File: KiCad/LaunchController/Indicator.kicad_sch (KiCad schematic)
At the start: 73 parts

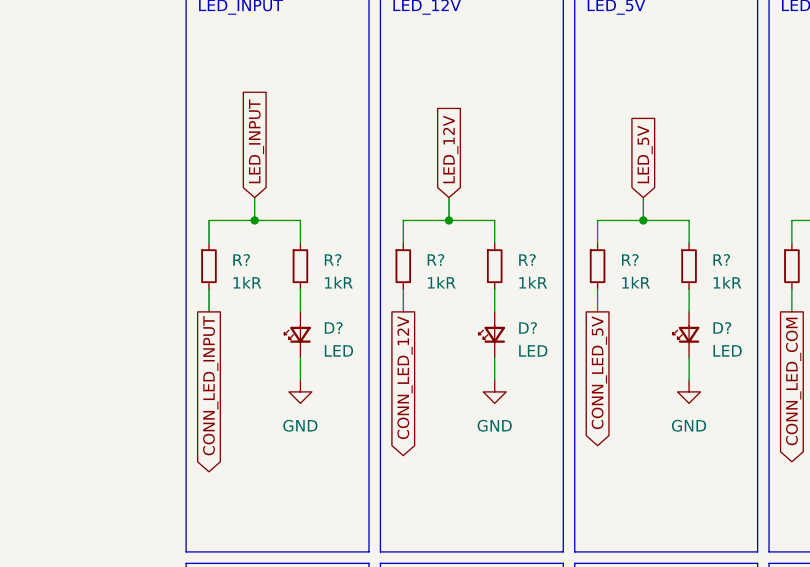
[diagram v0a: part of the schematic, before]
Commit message: 電圧から抵抗値を修正
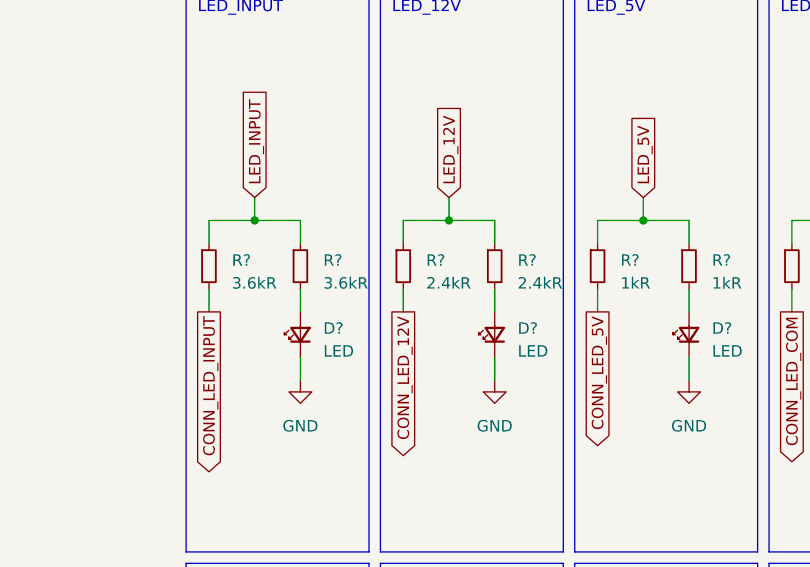
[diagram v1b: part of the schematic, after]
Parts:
- R? (x2): value 1kR -> 3.6kR
- R? (x2): value 1kR -> 2.4kR
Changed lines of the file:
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@@
       (effects (font (size 1.27 1.27)) (justify left))
     )
-    (property "Value" "1kR" (at 226.06 45.085 0)
+    (property "Value" "3.6kR" (at 226.06 45.085 0)
       (effects (font (size 1.27 1.27)) (justify left))
     )
@@
       (effects (font (size 1.27 1.27)) (justify left))
     )
-    (property "Value" "1kR" (at 215.9 45.085 0)
+    (property "Value" "3.6kR" (at 215.9 45.085 0)
       (effects (font (size 1.27 1.27)) (justify left))
     )
@@
       (effects (font (size 1.27 1.27)) (justify left))
     )
-    (property "Value" "1kR" (at 237.49 45.085 0)
+    (property "Value" "2.4kR" (at 237.49 45.085 0)
       (effects (font (size 1.27 1.27)) (justify left))
     )
@@
       (effects (font (size 1.27 1.27)) (justify left))
     )
-    (property "Value" "1kR" (at 247.65 45.085 0)
-      (effects (font (size 1.27 1.27)) (justify left))
-    )
+    (property "Value" "2.4kR" (at 247.65 45.085 0)
+      (effects (font (size 1.27 1.27)) (justify left))
+    )

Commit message: さらに分割
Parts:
- removed D? (x20): LED, LED_SMD:LED_0603_1608Metric_Pad1.05x0.95mm_HandSolder, symbol Device:LED_Small
- removed R? (x20): 1kR, Resistor_SMD:R_0603_1608Metric_Pad0.98x0.95mm_HandSolder, symbol Device:R_Small
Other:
- note removed: "LED_CLOSE"
- note removed: "LED_DUMP"
- note removed: "LED_EMERGENCY"
- note removed: "LED_FB_CLOSE"
- note removed: "LED_FB_DUMP"
- note removed: "LED_FB_FILL"
- note removed: "LED_FB_IGNITOR"
- note removed: "LED_FB_O2"
- note removed: "LED_FB_OPEN"
- note removed: "LED_FB_PURGE"
- note removed: "LED_FB_SHIFT"
- note removed: "LED_FILL"
- note removed: "LED_IGNITOR"
- note removed: "LED_O2"
- note removed: "LED_OPEN"
- note removed: "LED_POWER"
- note removed: "LED_PURGE"
- note removed: "LED_SAFTEY"
- note removed: "LED_SEQUENCE"
- note removed: "LED_SHIFT"
- moved on the sheet: D?, R?

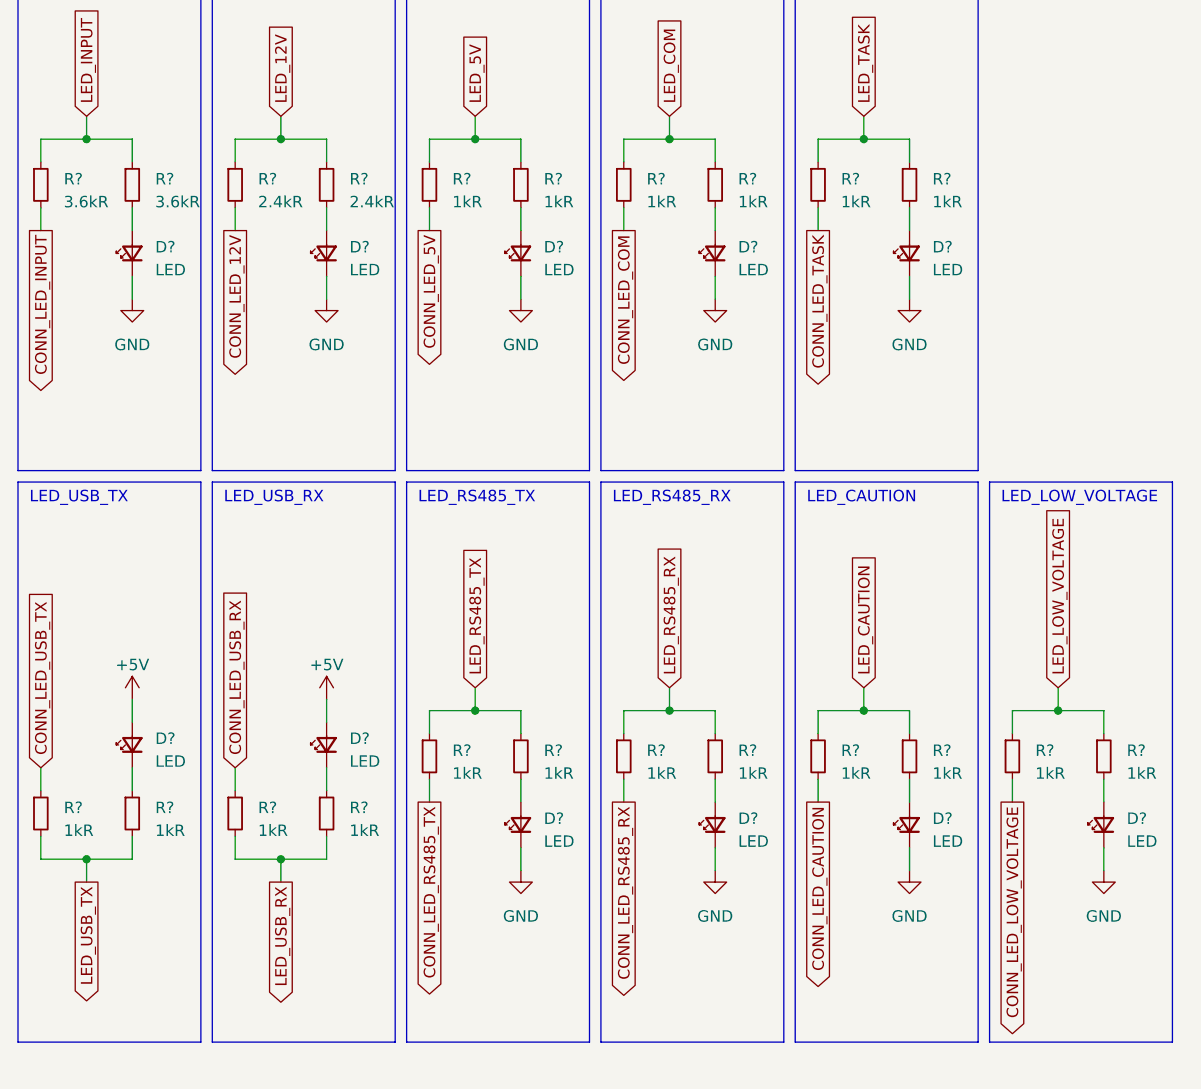
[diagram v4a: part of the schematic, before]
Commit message: あとはDRC解決とビア打ち
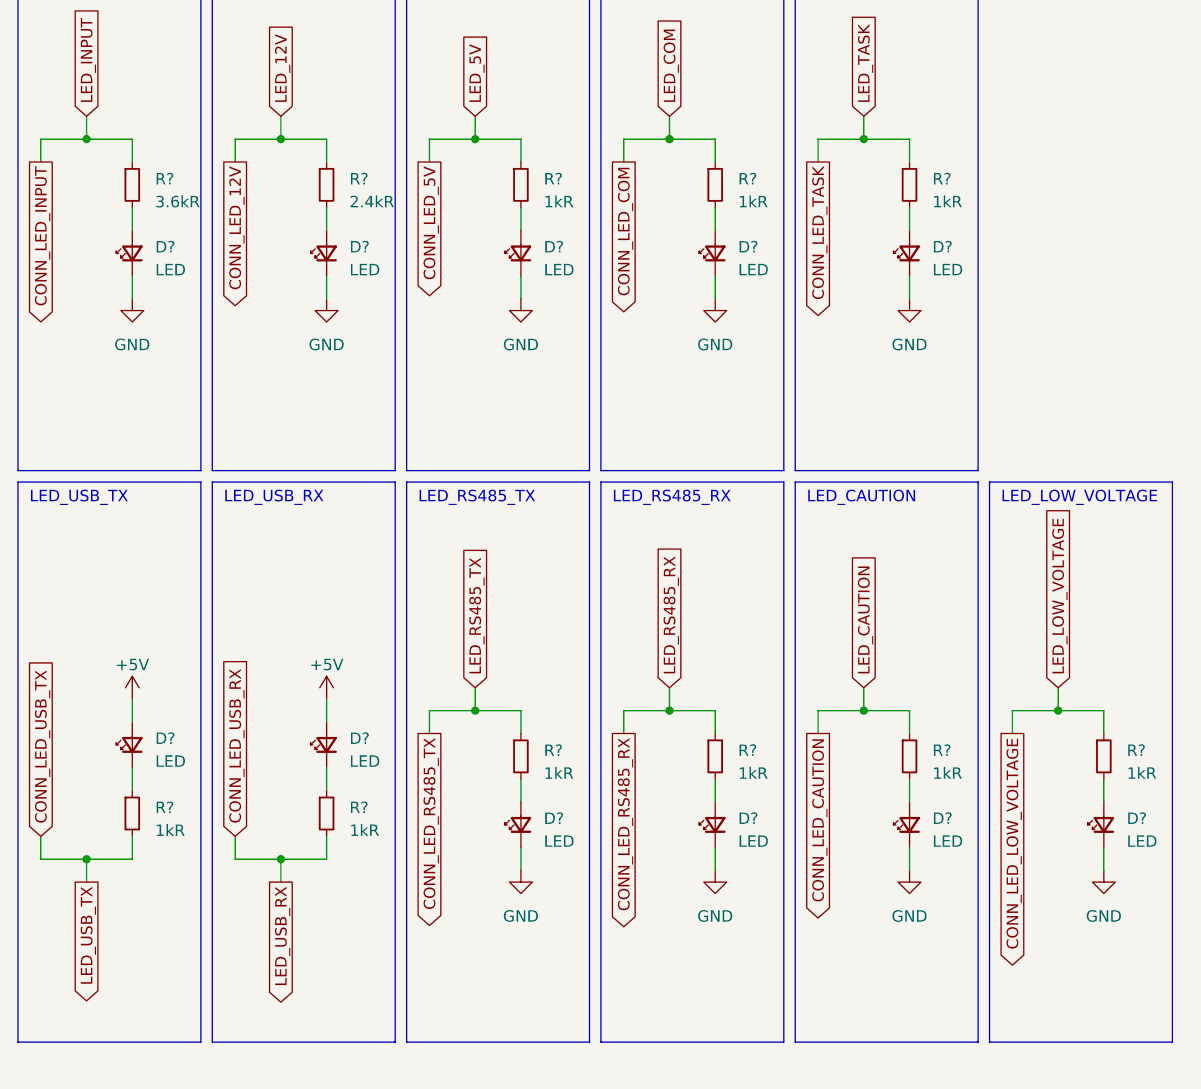
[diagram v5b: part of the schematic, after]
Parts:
- removed R? (x9): 1kR, Resistor_SMD:R_0603_1608Metric_Pad0.98x0.95mm_HandSolder, symbol Device:R_Small
- removed R?: 3.6kR, Resistor_SMD:R_0603_1608Metric_Pad0.98x0.95mm_HandSolder, symbol Device:R_Small
- removed R?: 2.4kR, Resistor_SMD:R_0603_1608Metric_Pad0.98x0.95mm_HandSolder, symbol Device:R_Small
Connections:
- net LED_12V is gone; now on net CONN_LED_12V: R?.1
- net LED_5V is gone; now on net CONN_LED_5V: R?.1
- net LED_CAUTION is gone; now on net CONN_LED_CAUTION: R?.1
- net LED_COM is gone; now on net CONN_LED_COM: R?.1
- net LED_INPUT is gone; now on net CONN_LED_INPUT: R?.1
- net LED_LOW_VOLTAGE is gone; now on net CONN_LED_LOW_VOLTAGE: R?.1
- net LED_RS485_RX is gone; now on net CONN_LED_RS485_RX: R?.1
- net LED_RS485_TX is gone; now on net CONN_LED_RS485_TX: R?.1
- net LED_TASK is gone; now on net CONN_LED_TASK: R?.1
- net LED_USB_RX is gone; now on net CONN_LED_USB_RX: R?.2
- net LED_USB_TX is gone; now on net CONN_LED_USB_TX: R?.2

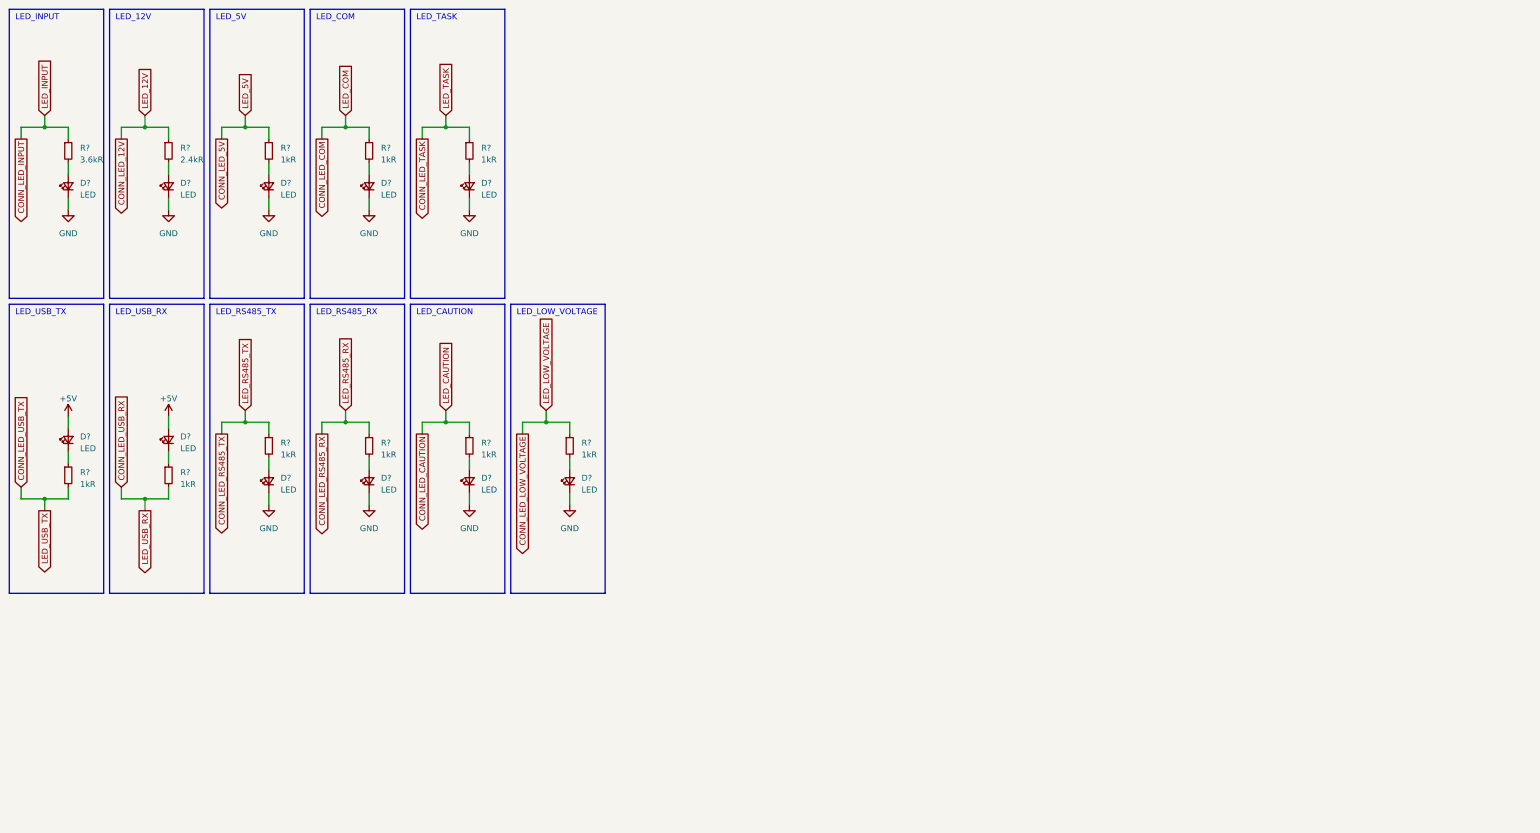
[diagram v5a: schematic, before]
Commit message: ジャンパーを回路図に追加
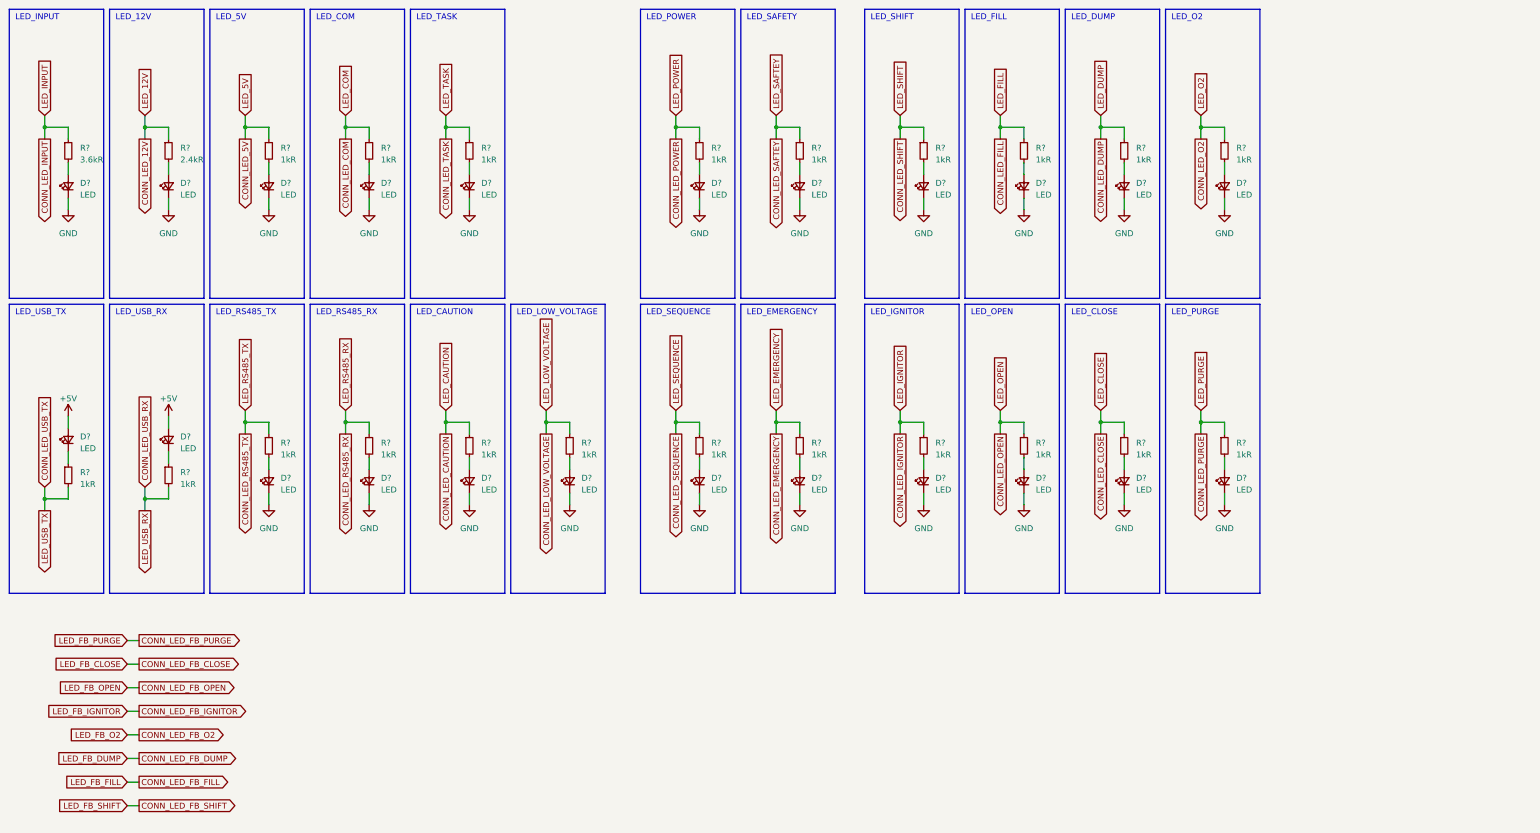
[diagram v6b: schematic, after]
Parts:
- added D? (x12): LED, LED_SMD:LED_0603_1608Metric_Pad1.05x0.95mm_HandSolder, symbol Device:LED_Small
- added R? (x12): 1kR, Resistor_SMD:R_0603_1608Metric_Pad0.98x0.95mm_HandSolder, symbol Device:R_Small
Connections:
- net GND: now also D?.1 (K), D?.1 (K), D?.1 (K), D?.1 (K), D?.1 (K), D?.1 (K), D?.1 (K), D?.1 (K), D?.1 (K), D?.1 (K), D?.1 (K), D?.1 (K)
- new net: D?.2 (A), R?.2 (x12)
- new net CONN_LED_CLOSE: R?.1
- new net CONN_LED_DUMP: R?.1
- new net CONN_LED_EMERGENCY: R?.1
- new net CONN_LED_FILL: R?.1
- new net CONN_LED_IGNITOR: R?.1
- new net CONN_LED_O2: R?.1
- new net CONN_LED_OPEN: R?.1
- new net CONN_LED_POWER: R?.1
- new net CONN_LED_PURGE: R?.1
- new net CONN_LED_SAFTEY: R?.1
- new net CONN_LED_SEQUENCE: R?.1
- new net CONN_LED_SHIFT: R?.1
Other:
- note added: "LED_CLOSE"
- note added: "LED_DUMP"
- note added: "LED_EMERGENCY"
- note added: "LED_FILL"
- note added: "LED_IGNITOR"
- note added: "LED_O2"
- note added: "LED_OPEN"
- note added: "LED_POWER"
- note added: "LED_PURGE"
- note added: "LED_SAFETY"
- note added: "LED_SEQUENCE"
- note added: "LED_SHIFT"
